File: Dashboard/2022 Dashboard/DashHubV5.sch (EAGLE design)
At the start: 32 parts, among them IC1 TLC5947DAPR, J1 LEFT, J2 RIGHT, J4 TBLH10-350-08BK, U1 ALLEGRO_MICROSYSTEMS_ACS722LL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

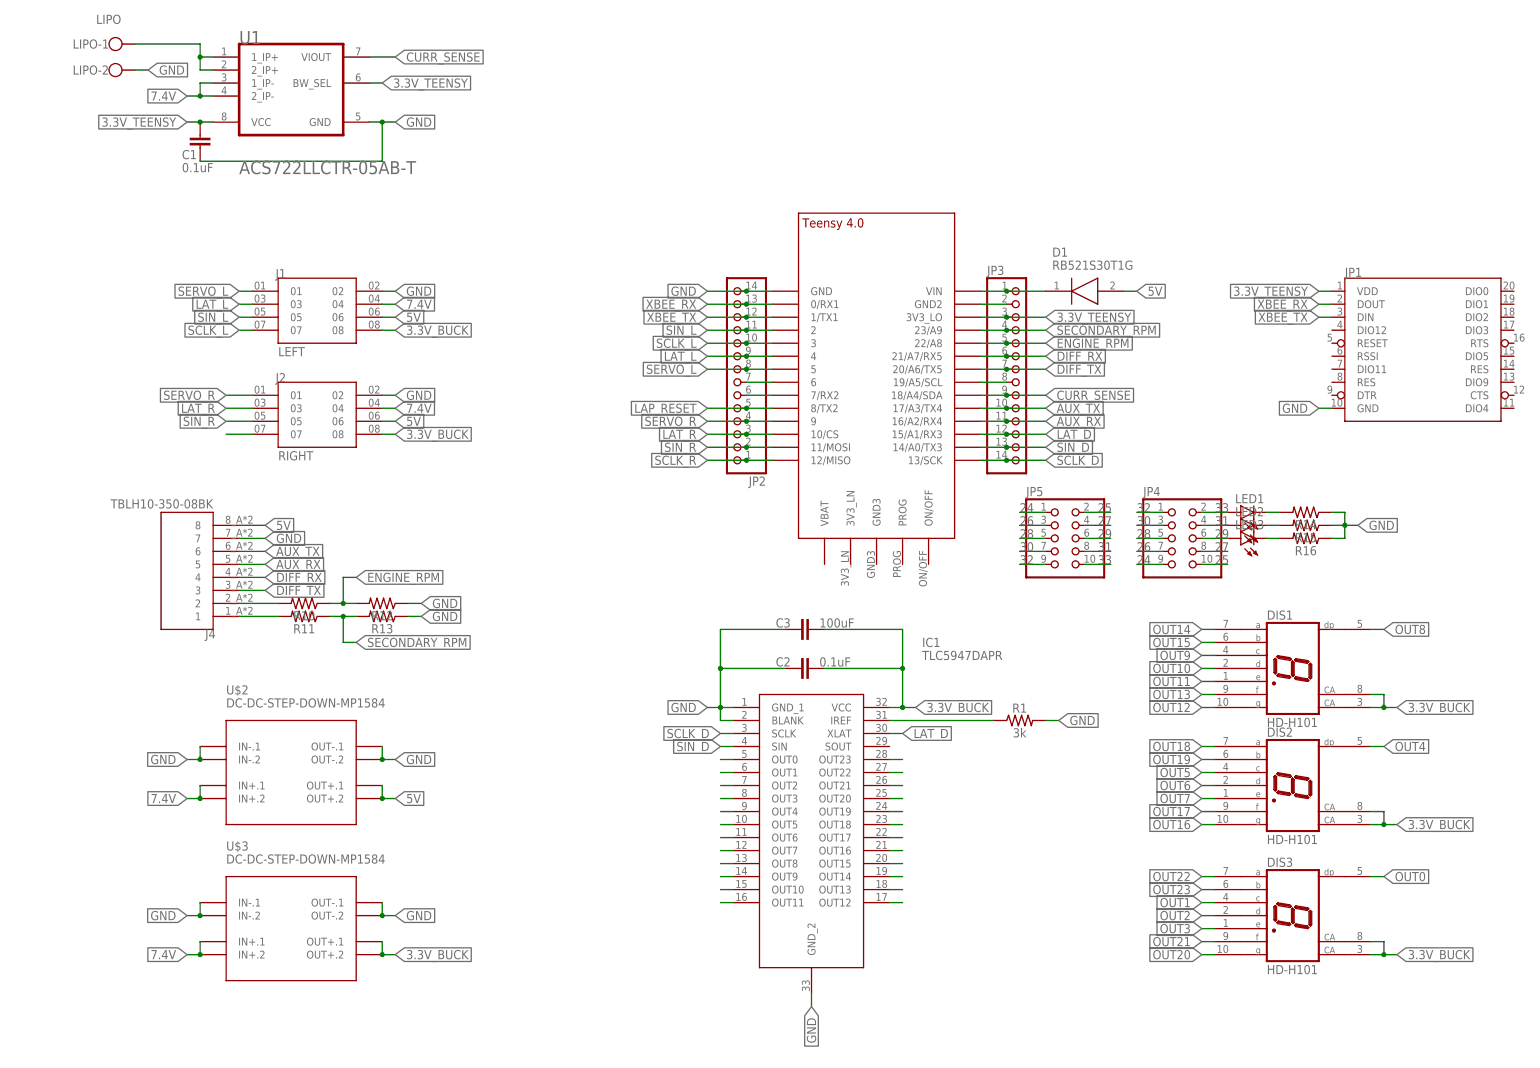
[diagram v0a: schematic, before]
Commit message: Updated all dashboard stuff
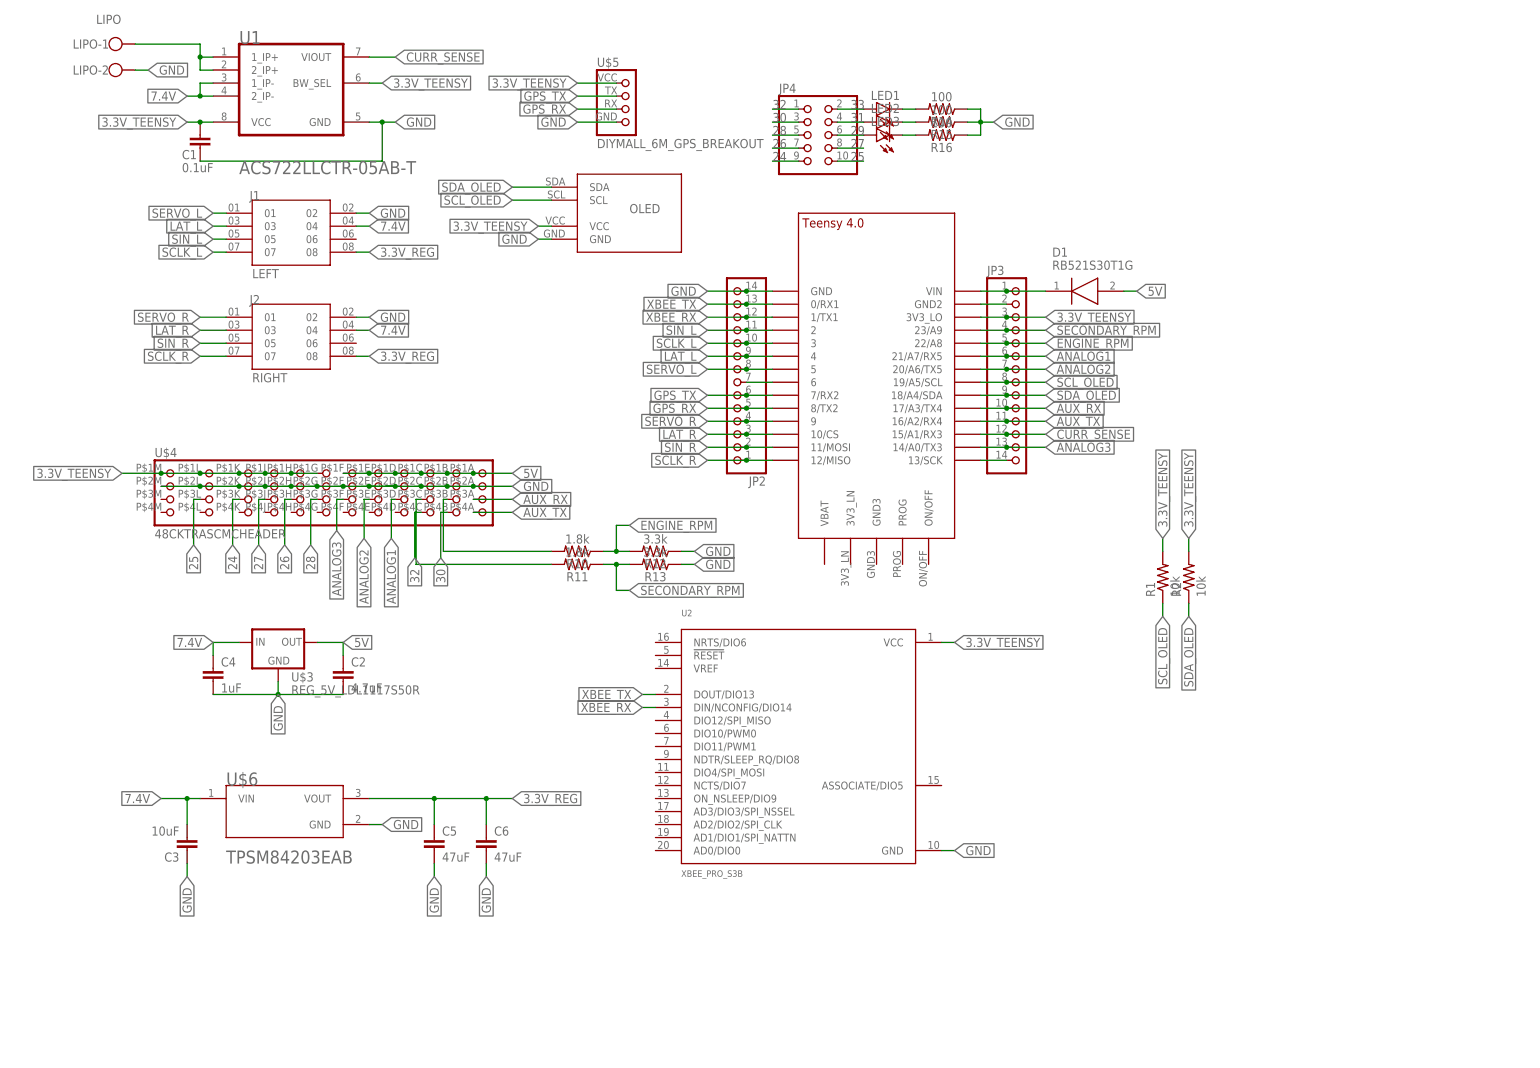
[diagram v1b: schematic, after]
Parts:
- removed DIS1, DIS2, DIS3: HD-H101, display-hp:HD-H101
- removed IC1: TLC5947DAPR, TLC5947DAPR:TLC5947DAPR
- removed J4: TBLH10-350-08BK, TBLH10-350-08BK:TBLH10-350-08BK
- removed JP1: (no value), SparkFun-RF:XBEE
- removed JP5: (no value), pinhead:PINHD-2X5
- added C4: 1uF, GTOR - Passive Components:CAP_SMDC1206
- added C5, C6: 47uF, GTOR - Passive Components:CAP_SMDC1206
- added R2: 10k, GTOR - Passive Components:RES_SMDR0603
- added U$4: 48CKTRASCMCHEADER, GTOR - Connectors:48CKTRASCMCHEADER
- added U$5: DIYMALL_6M_GPS_BREAKOUT, GTOR - Breakout Boards:DIYMALL_6M_GPS_BREAKOUT
- added U$6: TPSM84205EAB, GTOR - Active Components:TPSM84205EAB
- added U2: XBEE_PRO_S3B, GTOR - Microcontroller:XBEE_PRO_S3B
- C2: value 0.1uF -> 4.7uF; device rcl:C-EUC0402 -> GTOR - Passive Components:CAP_SMDC0603
- C3: value 100uF -> 10uF; device rcl:C-EUC1206 -> GTOR - Passive Components:CAP_SMDC1206
- R1: value 3k -> 10k; device SparkFun-Resistors:RESISTORAXIAL-0.3 -> GTOR - Passive Components:RES_SMDR0603
- R10, R11: value (none) -> 1.8k
- R12, R13: value (none) -> 3.3k
- R14, R15, R16: value (none) -> 100
- U$2: value DC-DC-STEP-DOWN-MP1584 -> OLED_SSD1306; device diy-modules:DC-DC-STEP-DOWN-MP1584 -> GTOR - Breakout Boards:OLED_SSD1306
- U$3: value DC-DC-STEP-DOWN-MP1584 -> REG_5V_LDL1117S50R; device diy-modules:DC-DC-STEP-DOWN-MP1584 -> GTOR - Active Components:REG_5V_LDL1117S50R
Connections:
- net N$17 renamed GND2
- removed net 3.3V_BUCK: C2.2, C3.2, DIS1.CA, DIS1.CA@1, DIS2.CA, DIS2.CA@1, DIS3.CA, DIS3.CA@1, IC1.VCC, J1.08, J2.08, U$3.OUT+.1, U$3.OUT+.2
- removed net DIFF_RX: J4.4, JP3.6, U$1.21/A7/RX5
- removed net DIFF_TX: J4.3, JP3.7, U$1.20/A6/TX5
- removed net LAP_RESET: JP2.5, U$1.8/TX2
- removed net LAT_D: IC1.XLAT, JP3.12, U$1.15/A1/RX3
- removed net N$28: IC1.IREF, R1.1
- removed net N$3: JP2.6, U$1.7/RX2
- removed net N$4: JP3.8, U$1.19/A5/SCL
- removed net OUT0: DIS3.DP, IC1.OUT0
- removed net OUT1: DIS3.C, IC1.OUT1
- removed net OUT10: DIS1.D, IC1.OUT10
- removed net OUT11: DIS1.E, IC1.OUT11
- removed net OUT12: DIS1.G, IC1.OUT12
- removed net OUT13: DIS1.F, IC1.OUT13
- removed net OUT14: DIS1.A, IC1.OUT14
- removed net OUT15: DIS1.B, IC1.OUT15
- removed net OUT16: DIS2.G, IC1.OUT16
- removed net OUT17: DIS2.F, IC1.OUT17
- removed net OUT18: DIS2.A, IC1.OUT18
- removed net OUT19: DIS2.B, IC1.OUT19
- removed net OUT2: DIS3.D, IC1.OUT2
- removed net OUT20: DIS3.G, IC1.OUT20
- removed net OUT21: DIS3.F, IC1.OUT21
- removed net OUT22: DIS3.A, IC1.OUT22
- removed net OUT23: DIS3.B, IC1.OUT23
- removed net OUT3: DIS3.E, IC1.OUT3
- removed net OUT4: DIS2.DP, IC1.OUT4
- removed net OUT5: DIS2.C, IC1.OUT5
- removed net OUT6: DIS2.D, IC1.OUT6
- removed net OUT7: DIS2.E, IC1.OUT7
- removed net OUT8: DIS1.DP, IC1.OUT8
- removed net OUT9: DIS1.C, IC1.OUT9
- removed net SIN_D: IC1.SIN, JP3.13, U$1.14/A0/TX3
- new net 3.3V_REG: C5.1, C6.1, J1.08, J2.08, U$6.VOUT
- new net ANALOG1: JP3.6, U$1.21/A7/RX5, U$4.3D
- new net ANALOG2: JP3.7, U$1.20/A6/TX5, U$4.3E
- new net ANALOG3: JP3.13, U$1.14/A0/TX3, U$4.3F
- new net GPS_RX: JP2.5, U$1.8/TX2, U$5.RX
- new net GPS_TX: JP2.6, U$1.7/RX2, U$5.TX
- new net SCL_OLED: JP3.8, R1.1, U$1.19/A5/SCL, U$2.SCL
- new net SDA_OLED: JP3.9, R2.1, U$1.18/A4/SDA, U$2.SDA
- net 24: now also U$4.3K; no longer JP5.1
- net 25: now also U$4.3L; no longer JP5.2
- net 26: now also U$4.3H; no longer JP5.3
- net 27: now also U$4.3J; no longer JP5.4
- net 28: now also U$4.3G; no longer JP5.5
- net 29: no longer JP5.6
- net 3.3V_TEENSY: now also R1.2, R2.2, U$2.VCC, U$4.1G, U$4.1H, U$4.1J, U$4.1K, U$4.1L, U$4.1M, U$5.VCC, U2.VCC; no longer JP1.VDD
- net 30: now also U$4.4B; no longer JP5.7
- net 31: no longer JP5.8
- net 32: now also U$4.4C; no longer JP5.9
- net 33: no longer JP5.10
- net 5V: now also C2.1, U$3.OUT, U$4.1A, U$4.1B, U$4.1C, U$4.1D, U$4.1E, U$4.1F; no longer J1.06, J2.06, J4.8, U$2.OUT+.1, U$2.OUT+.2
- net 7.4V: now also C3.2, C4.1, U$3.IN, U$6.VIN; no longer U$2.IN+.1, U$2.IN+.2, U$3.IN+.1, U$3.IN+.2
- net AUX_RX: now also JP3.10, U$1.17/A3/TX4, U$4.3A; no longer J4.5, JP3.11, U$1.16/A2/RX4
- net AUX_TX: now also JP3.11, U$1.16/A2/RX4, U$4.4A; no longer J4.6, JP3.10, U$1.17/A3/TX4
- net CURR_SENSE: now also JP3.12, U$1.15/A1/RX3; no longer JP3.9, U$1.18/A4/SDA
- net GND: now also C2.2, C4.2, C5.2, C6.2, U$2.GND, U$3.GND, U$4.2A, U$4.2B, U$4.2C, U$4.2D, U$4.2E, U$4.2F, U$4.2G, U$4.2H, U$4.2J, U$4.2K, U$4.2L, U$4.2M, U$5.GND, U$6.GND, U2.GND; no longer C2.1, IC1.BLANK, IC1.GND_1, IC1.GND_2, J4.7, JP1.GND, R1.2, U$2.IN-.1, U$2.IN-.2, U$2.OUT-.1, U$2.OUT-.2, U$3.IN-.1, U$3.IN-.2, U$3.OUT-.1, U$3.OUT-.2
- net N$23: now also U$4.3B; no longer J4.2
- net N$24: now also U$4.3C; no longer J4.1
- net SCLK_D: no longer IC1.SCLK
- net XBEE_RX: now also JP2.12, U$1.1/TX1, U2.DIN/NCONFIG/DIO14; no longer JP1.DOUT, JP2.13, U$1.0/RX1
- net XBEE_TX: now also JP2.13, U$1.0/RX1, U2.DOUT/DIO13; no longer JP1.DIN, JP2.12, U$1.1/TX1
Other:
- note added: "Pull up resistors"
- moved on the sheet: C2, C3, J1, J2, JP4, LED1, LED2, LED3, R1, R10, R11, R12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
